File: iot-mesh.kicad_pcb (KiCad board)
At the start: 2 copper layers, 73 x 39 mm, 18 parts, among them J1 DS18B20 connector, J2 BME280 connector, J5 Power Connector, U1 XIAO-nRF52840-DIP, U2 WEMOS_D1_mini, U3 L7805

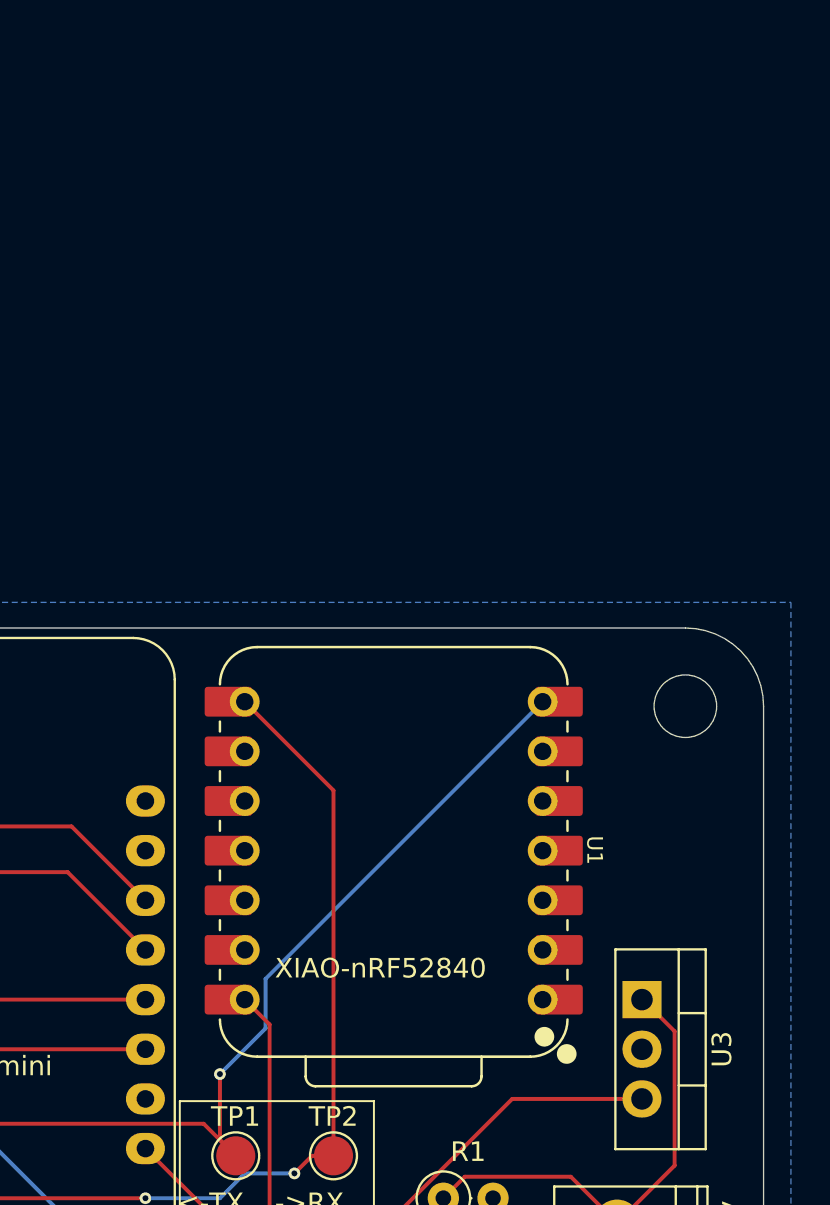
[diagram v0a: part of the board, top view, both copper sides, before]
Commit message: Add pin headers for nRF
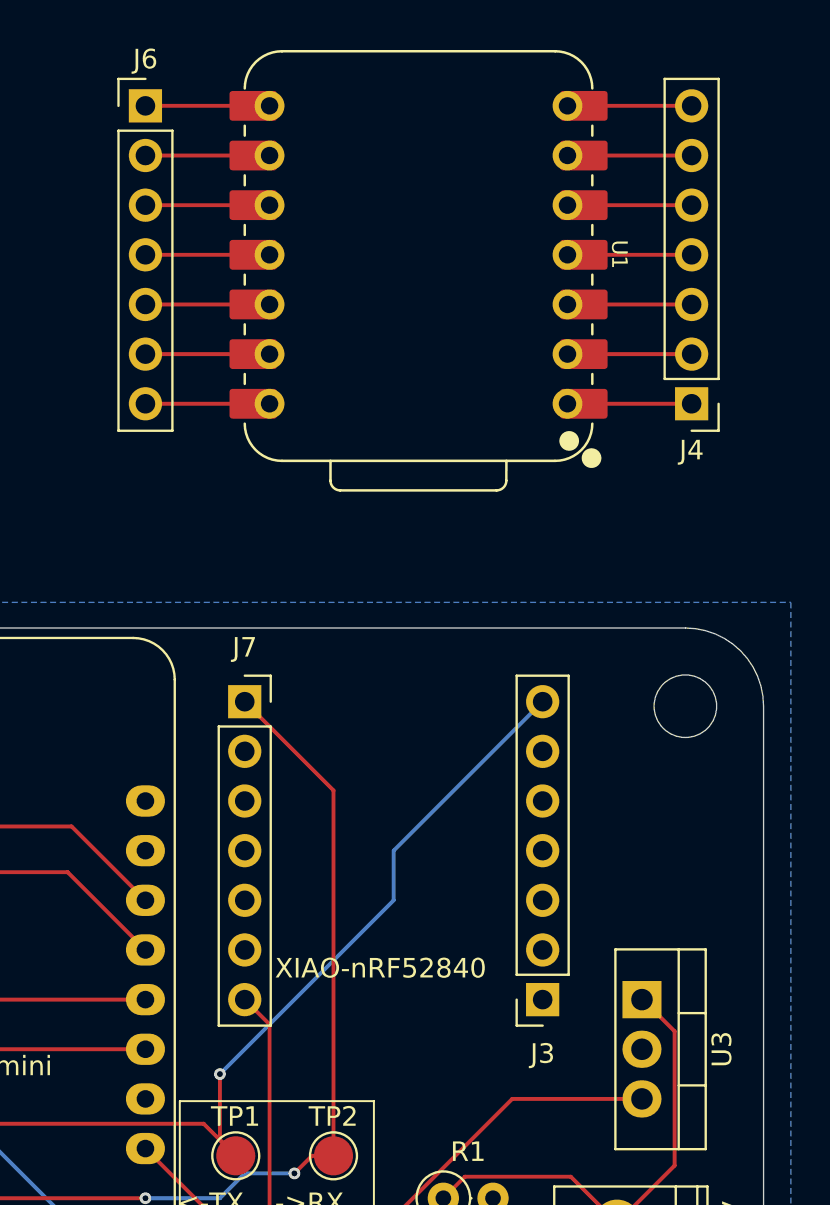
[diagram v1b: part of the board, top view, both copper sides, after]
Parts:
- added J3: Conn_01x07_Socket, Connector_PinSocket_2.54mm:PinSocket_1x07_P2.54mm_Vertical, F.Cu at (139.7, 80.0)
- added J4: Conn_01x07_Pin, Connector_PinHeader_2.54mm:PinHeader_1x07_P2.54mm_Vertical, F.Cu at (147.3, 49.5)
- added J6: Conn_01x07_Pin, Connector_PinHeader_2.54mm:PinHeader_1x07_P2.54mm_Vertical, F.Cu at (119.4, 34.3)
- added J7: Conn_01x07_Socket, Connector_PinSocket_2.54mm:PinSocket_1x07_P2.54mm_Vertical, F.Cu at (124.5, 64.8)
- moved U1 30.5 mm to (133.3, 41.9)
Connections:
- JP2 pad 1: Net-(JP2-A) -> Net-(J7-Pin_7)
- TP1 pad 1: Net-(U1-P1.11_D6_TX) -> /nRF_TX
- TP2 pad 1: Net-(U1-P1.12_D7_RX) -> Net-(J7-Pin_1)
- U1 pad 1: unconnected-(U1-P0.02_A0_D0-Pad1) -> Net-(J4-Pin_1)
- U1 pad 10: unconnected-(U1-P1.14_D9_MISO-Pad10) -> Net-(J6-Pin_3)
- U1 pad 11: unconnected-(U1-P1.15_D10_MOSI-Pad11) -> Net-(J6-Pin_4)
- U1 pad 12: unconnected-(U1-3V3-Pad12)_1 -> Net-(J6-Pin_5)
- U1 pad 13: GND -> Net-(J6-Pin_6)
- U1 pad 14: Net-(JP2-A) -> Net-(J6-Pin_7)
- U1 pad 2: unconnected-(U1-P0.03_A1_D1-Pad2) -> Net-(J4-Pin_2)
- U1 pad 3: unconnected-(U1-P0.28_A2_D2-Pad3) -> Net-(J4-Pin_3)
- U1 pad 4: unconnected-(U1-P0.29_A3_D3-Pad4)_1 -> Net-(J4-Pin_4)
- U1 pad 5: unconnected-(U1-P0.04_A4_D4_SDA-Pad5) -> Net-(J4-Pin_5)
- U1 pad 6: unconnected-(U1-P0.05_A5_D5_SCL-Pad6)_1 -> Net-(J4-Pin_6)
- U1 pad 7: Net-(U1-P1.11_D6_TX) -> Net-(J4-Pin_7)
- U1 pad 8: Net-(U1-P1.12_D7_RX) -> /nRF_RX
- U1 pad 9: unconnected-(U1-P1.13_D8_SCK-Pad9) -> Net-(J6-Pin_2)
- U2 pad 6: Net-(U1-P1.11_D6_TX) -> /nRF_TX
- U2 pad 7: Net-(U1-P1.12_D7_RX) -> Net-(J7-Pin_1)
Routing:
- net Net-(U1-P1.12_D7_RX): track 60.6 -> 0.00 mm, vias 2 -> 0
- net Net-(J7-Pin_1): track 0.00 -> 60.6 mm, vias 0 -> 2
- net /nRF_TX: track 0.00 -> 60.1 mm, vias 0 -> 1
- net Net-(U1-P1.11_D6_TX): track 60.1 -> 0.00 mm, vias 1 -> 0
- net Net-(JP2-A): track 15.5 -> 0.00 mm
- net Net-(J7-Pin_7): track 0.00 -> 15.5 mm
- net Net-(J6-Pin_7): track 0.00 -> 6.35 mm
- net Net-(J6-Pin_6): track 0.00 -> 6.35 mm
- net Net-(J6-Pin_5): track 0.00 -> 6.35 mm
- net Net-(J6-Pin_4): track 0.00 -> 6.35 mm
- net Net-(J6-Pin_3): track 0.00 -> 6.35 mm
- net Net-(J6-Pin_2): track 0.00 -> 6.35 mm
- net /nRF_RX: track 0.00 -> 6.35 mm
- net Net-(J4-Pin_7): track 0.00 -> 6.35 mm
- net Net-(J4-Pin_6): track 0.00 -> 6.35 mm
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
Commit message: 
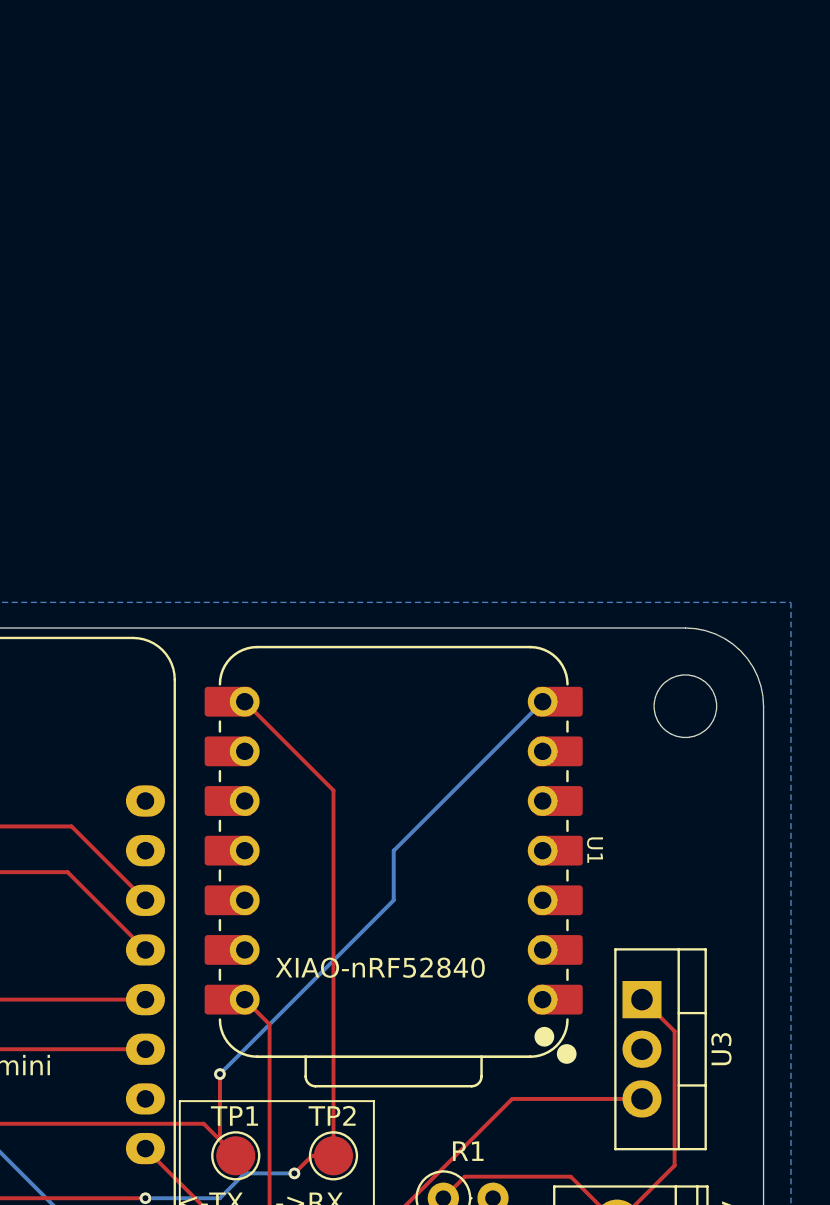
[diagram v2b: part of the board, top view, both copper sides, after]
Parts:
- removed J3, J7: Conn_01x07_Socket, Connector_PinSocket_2.54mm:PinSocket_1x07_P2.54mm_Vertical
- removed J4, J6: Conn_01x07_Pin, Connector_PinHeader_2.54mm:PinHeader_1x07_P2.54mm_Vertical
- moved U1 30.5 mm to (132.1, 72.4)
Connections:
- JP2 pad 1: Net-(J7-Pin_7) -> Net-(JP2-A)
- TP1 pad 1: /nRF_TX -> /nRF TX
- TP2 pad 1: Net-(J7-Pin_1) -> /nRF RX
- U1 pad 1: Net-(J4-Pin_1) -> unconnected-(U1-P0.02_A0_D0-Pad1)
- U1 pad 10: Net-(J6-Pin_3) -> unconnected-(U1-P1.14_D9_MISO-Pad10)_1
- U1 pad 11: Net-(J6-Pin_4) -> unconnected-(U1-P1.15_D10_MOSI-Pad11)_1
- U1 pad 12: Net-(J6-Pin_5) -> unconnected-(U1-3V3-Pad12)
- U1 pad 13: Net-(J6-Pin_6) -> GND
- U1 pad 14: Net-(J6-Pin_7) -> Net-(JP2-A)
- U1 pad 2: Net-(J4-Pin_2) -> unconnected-(U1-P0.03_A1_D1-Pad2)
- U1 pad 3: Net-(J4-Pin_3) -> unconnected-(U1-P0.28_A2_D2-Pad3)_1
- U1 pad 4: Net-(J4-Pin_4) -> unconnected-(U1-P0.29_A3_D3-Pad4)
- U1 pad 5: Net-(J4-Pin_5) -> unconnected-(U1-P0.04_A4_D4_SDA-Pad5)
- U1 pad 6: Net-(J4-Pin_6) -> unconnected-(U1-P0.05_A5_D5_SCL-Pad6)_1
- U1 pad 7: Net-(J4-Pin_7) -> /nRF TX
- U1 pad 8: /nRF_RX -> /nRF RX
- U1 pad 9: Net-(J6-Pin_2) -> unconnected-(U1-P1.13_D8_SCK-Pad9)_1
- U2 pad 6: /nRF_TX -> /nRF TX
- U2 pad 7: Net-(J7-Pin_1) -> /nRF RX
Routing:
- net Net-(J7-Pin_1): track 60.6 -> 0.00 mm, vias 2 -> 0
- net /nRF RX: track 0.00 -> 60.6 mm, vias 0 -> 2
- net /nRF_TX: track 60.1 -> 0.00 mm, vias 1 -> 0
- net /nRF TX: track 0.00 -> 60.1 mm, vias 0 -> 1
- net Net-(JP2-A): track 0.00 -> 15.5 mm
- net Net-(J7-Pin_7): track 15.5 -> 0.00 mm
- net Net-(J6-Pin_7): track 6.35 -> 0.00 mm
- net Net-(J6-Pin_6): track 6.35 -> 0.00 mm
- net Net-(J6-Pin_5): track 6.35 -> 0.00 mm
- net Net-(J6-Pin_4): track 6.35 -> 0.00 mm
- net Net-(J6-Pin_3): track 6.35 -> 0.00 mm
- net Net-(J6-Pin_2): track 6.35 -> 0.00 mm
- net /nRF_RX: track 6.35 -> 0.00 mm
- net Net-(J4-Pin_7): track 6.35 -> 0.00 mm
- net Net-(J4-Pin_6): track 6.35 -> 0.00 mm
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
